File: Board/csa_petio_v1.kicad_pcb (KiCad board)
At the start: 2 copper layers, 160 x 100 mm, 99 parts, among them IC16 74LVC8T245SO24, J1 DIN-6, J11 Conn_01x09, J12 Conn_01x09, J14 Extended_PET_keyboard_connect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, J2 Conn_01x23, P1 PETUSERPORT, P2 IEEE488FLATCABLE, P4 CSABUS, P5 CBMTAPE, U1 XC6SLX9-TQG144, U10 74LS06, U11 SN74LVC245APW, U12 4051, U13 4051, U14 74LVC1G04, U15 ADM560, U16 LSF0204Q, U17 LSF0204Q, U18 LSF0204Q, U19 LSF0204Q, U2 SN74LVC245APW, U21 74LVC1G125, U22 74LVC1G125, U23 74LVC1G00, U3 SN74LVC245APW, U4 SN75160BDW, U5 SN75161BDW, U6 LSF0204Q, U7 LSF0204Q, U8 LSF0204Q, U9 LSF0204Q, X3 M09HPS

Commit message: start working on 1.0b
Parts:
- IC16: footprint Package_SO:TSSOP-24_6.1x7.8mm_P0.65mm -> Package_SO:TSSOP-24_4.4x7.8mm_P0.65mm
- R5: value 4k7 -> 10k
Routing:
- net GND: track 943.6 -> 945.3 mm
- net VCC: track 754.8 -> 755.7 mm
- net R/-W: track 54.5 -> 55.3 mm
- net Net-(IC16-B8): track 32.4 -> 33.2 mm
- net Net-(IC16-B7): track 31.6 -> 32.4 mm
- net Net-(IC16-B6): track 29.0 -> 29.9 mm
- net Net-(IC16-B5): track 27.9 -> 28.8 mm
- net Net-(IC16-B4): track 26.9 -> 27.8 mm
- net Net-(IC16-B3): track 24.9 -> 25.7 mm
- net Net-(IC16-B2): track 24.0 -> 24.9 mm
- net Net-(IC16-B1): track 25.2 -> 26.0 mm
- net D7: track 18.2 -> 19.1 mm
- net D6: track 18.0 -> 18.9 mm
- net D5: track 18.0 -> 18.8 mm
- net D4: track 18.3 -> 19.2 mm
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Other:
- board text added: "CSA-CBMIO-V1.0B"
- board text removed: "CSA-CBMIO-V1.0A"

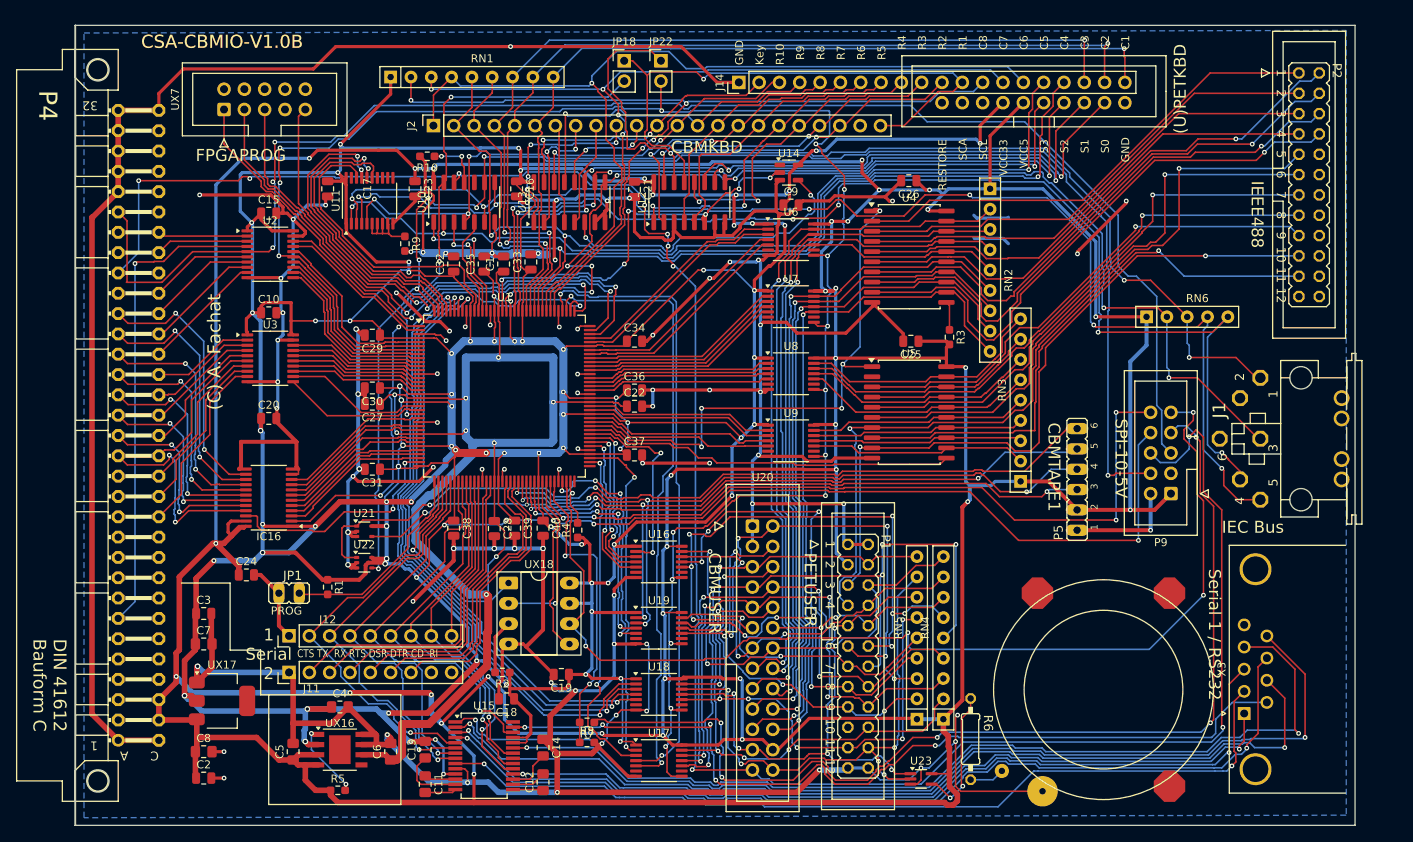
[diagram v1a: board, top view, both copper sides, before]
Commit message: schem draft done, layout work started
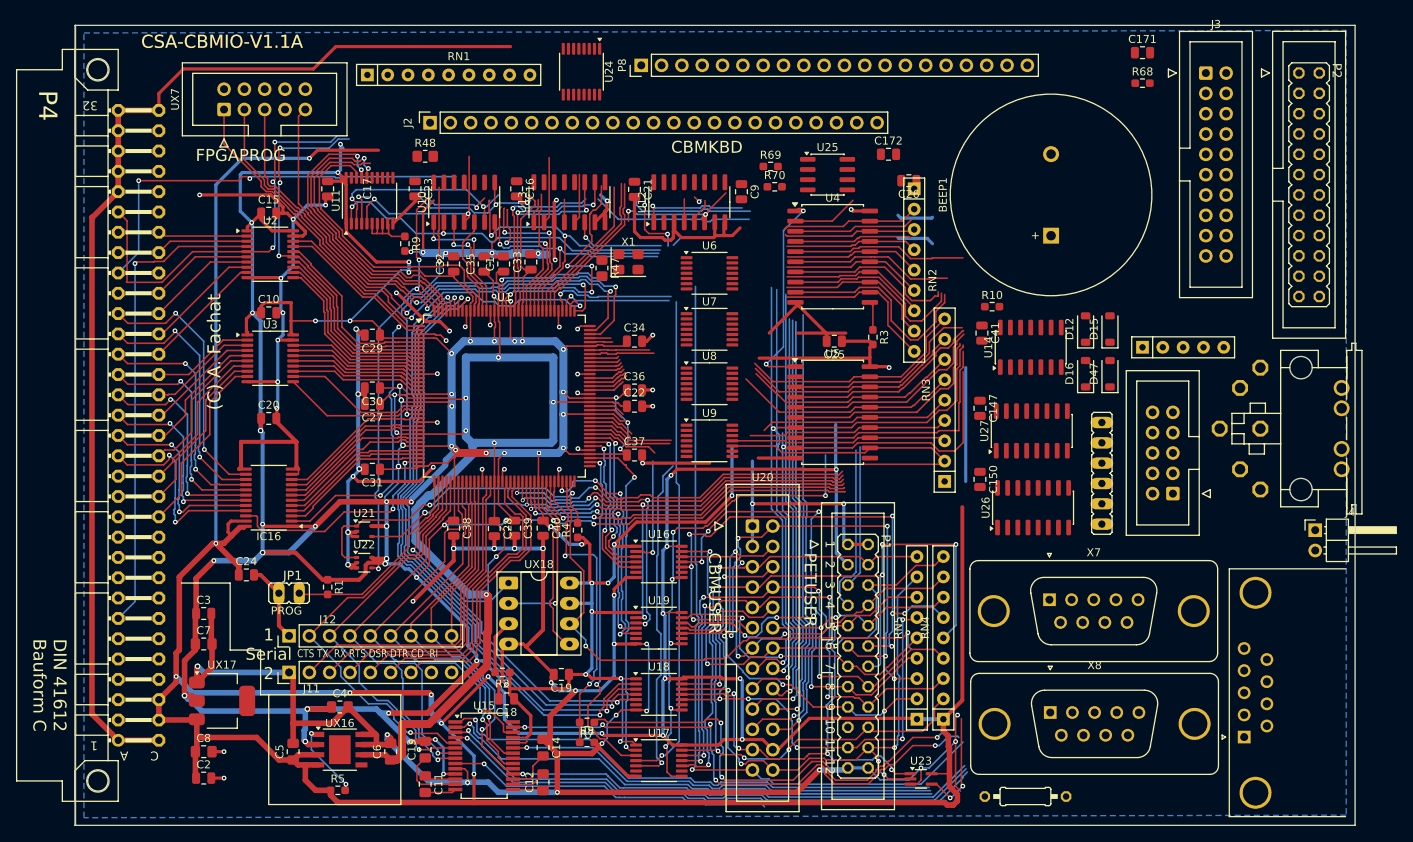
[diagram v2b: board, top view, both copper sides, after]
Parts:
- removed J14: Extended_PET_keyboard_connector, csa_petio_v1:PET_Extended_Keyboard_Connector
- removed JP18, JP22: JP1E, Connector_PinHeader_2.54mm:PinHeader_1x02_P2.54mm_Vertical
- added C147: 0.1u, Capacitor_SMD:C_0805_2012Metric, F.Cu at (181.6, 102.9)
- added C150: 0.1u, Capacitor_SMD:C_0805_2012Metric, F.Cu at (181.6, 111.8)
- added C171: 51pF, Capacitor_SMD:C_0805_2012Metric, F.Cu at (201.9, 58.4)
- added C172: 360p, Capacitor_SMD:C_0805_2012Metric, F.Cu at (170.2, 71.1)
- added C41: 100n, Capacitor_SMD:C_0805_2012Metric, F.Cu at (181.9, 93.5)
- added D12: 1N4448, Diode_SMD:D_SOD-123, F.Cu at (194.8, 93.0)
- added D15: 1N4448, Diode_SMD:D_SOD-123, F.Cu at (197.9, 93.0)
- added D16: 1N4448, Diode_SMD:D_SOD-123, F.Cu at (194.8, 98.6)
- added D47: 1N4448, Diode_SMD:D_SOD-123, F.Cu at (197.9, 98.6)
- added J3: New_PET_keyboard_connector, Connector_IDC:IDC-Header_2x10_P2.54mm_Vertical, F.Cu at (209.8, 61.0)
- added J4: Conn_01x02, Connector_PinHeader_2.54mm:PinHeader_1x02_P2.54mm_Horizontal, F.Cu at (223.5, 118.1)
- added P8: ~, Connector_PinHeader_2.54mm:PinHeader_1x20_P2.54mm_Vertical, F.Cu at (139.3, 60.0)
- added R47: 4k7, Resistor_SMD:R_0805_2012Metric_Pad1.20x1.40mm_HandSolder, F.Cu at (134.4, 85.3)
- added R48: 4k7, Resistor_SMD:R_0805_2012Metric_Pad1.20x1.40mm_HandSolder, F.Cu at (112.3, 71.4)
- added R68: 1M, Resistor_SMD:R_0603_1608Metric_Pad0.98x0.95mm_HandSolder, F.Cu at (201.9, 62.2)
- added R69: 1M, Resistor_SMD:R_0603_1608Metric_Pad0.98x0.95mm_HandSolder, F.Cu at (155.4, 72.6)
- added R70: 47k, Resistor_SMD:R_0603_1608Metric_Pad0.98x0.95mm_HandSolder, F.Cu at (156.0, 75.2)
- added U24: 74LVC165, Package_SO:TSSOP-16_4.4x5mm_P0.65mm, F.Cu at (131.8, 60.8)
- added U25: NE555D, Package_SO:SOIC-8_3.9x4.9mm_P1.27mm, F.Cu at (162.6, 73.7)
- added U26: CD4053B, Package_SO:SOIC-16_3.9x9.9mm_P1.27mm, F.Cu at (188.2, 115.3)
- added U27: CD4053B, Package_SO:SOIC-16_3.9x9.9mm_P1.27mm, F.Cu at (188.1, 105.7)
- added X1: 18.432MHz, Oscillator:Oscillator_SMD_SeikoEpson_SG8002CE-4Pin_3.2x2.5mm, F.Cu at (137.7, 84.6)
- added X7: M09-182, Connector_Dsub:DSUB-9_Pins_Vertical_P2.77x2.84mm_MountingHoles, F.Cu at (190.3, 126.8)
- added X8: M09-182, Connector_Dsub:DSUB-9_Pins_Vertical_P2.77x2.84mm_MountingHoles, F.Cu at (190.4, 140.9)
- BEEP1: footprint csa_petio_v1:PIEZOBEEPER -> Buzzer_Beeper:MagneticBuzzer_StarMicronics_TMX-H
- R10, R3, R9: value 1k -> 4k7
- U14: value 74LVC1G04 -> 74LS06; footprint Package_TO_SOT_SMD:SOT-23-5 -> Package_SO:SO-14_3.9x8.65mm_P1.27mm
- moved R10 73.1 mm to (183.1, 90.2), turned to 0 degrees
- moved BEEP1 57.1 mm to (190.5, 81.3)
- moved U14 37.3 mm to (188.0, 95.2), turned to 90 degrees
- moved U6 11.0 mm to (147.8, 86.0)
- moved U7 10.6 mm to (147.8, 93.0)
- moved U8 10.3 mm to (147.8, 99.8)
- moved U9 10.2 mm to (147.8, 106.9)
- moved R6 9.93 mm to (187.3, 151.4), turned to 0 degrees
- moved R3 9.57 mm to (168.2, 94.0)
- moved U4 9.57 mm to (163.2, 83.9)
- moved U5 9.57 mm to (163.2, 103.4)
- moved C25 9.57 mm to (163.4, 94.5)
- moved RN2 9.49 mm to (173.4, 75.4)
- moved RN3 9.49 mm to (177.2, 112.0)
- moved C9 6.41 mm to (151.8, 75.8), turned to -90 degrees
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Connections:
- net Net-(P1-PA0) renamed PUP0
- net Net-(P1-PA1) renamed PUP1
- net Net-(P1-PA2) renamed PUP2
- net Net-(P1-PA3) renamed PUP3
- net Net-(P1-PA4) renamed PUP4
- net Net-(P1-PA5) renamed PUP5
- net Net-(P1-PA6) renamed PUP6
- net Net-(P1-PA7) renamed PUP7
- P4 pad A23: unconnected-(P4-/NMI-PadA23) -> /BNMI
- R10 pad 1: Net-(R10-Pad1) -> VCC
- R10 pad 2: GND -> Net-(R10-Pad2)
- RN1 pad 2: Net-(RN1-R1) -> Net-(J3-C8)
- RN1 pad 3: Net-(RN1-R2) -> Net-(J3-C7)
- U1 pad 1: PHI2 -> /IRQ
- U1 pad 114: Net-(RN1-R1) -> unconnected-(U1A-IO_L65N_SCP2_0-Pad114)
- U1 pad 115: Net-(RN1-R2) -> unconnected-(U1A-IO_L65P_SCP3_0-Pad115)
- U1 pad 116: Net-(J2-Pin_1) -> UP14
- U1 pad 117: Net-(J2-Pin_2) -> Net-(U1A-IO_L64P_SCP5_0)
- U1 pad 118: Net-(J2-Pin_3) -> Net-(U1A-IO_L63N_SCP6_0)
- U1 pad 119: Net-(J2-Pin_4) -> Net-(U1A-IO_L63P_SCP7_0)
- U1 pad 120: Net-(J2-Pin_5) -> Net-(U1A-IO_L62N_VREF_0)
- U1 pad 121: Net-(J2-Pin_6) -> Net-(U1A-IO_L62P_0)
- U1 pad 23: /IRQ -> PHI2
- U10 pad 10: unconnected-(U10-Pad10) -> Net-(U13-Inh)
- U10 pad 11: Net-(R10-Pad1) -> KSEL3
- U14 pad 1: (no net) -> Net-(U1A-IO_L64P_SCP5_0)
- U14 pad 2: KSEL3 -> NDAC
- U14 pad 3: GND -> Net-(U1A-IO_L64P_SCP5_0)
- U14 pad 4: Net-(U13-Inh) -> NRFD
- U14 pad 5: V33 -> Net-(U25-Q)
- UX7 pad 10: (no net) -> GND
- UX7 pad 2: (no net) -> GND
- UX7 pad 4: (no net) -> V33
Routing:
- net VCC: track 755.7 -> 519.0 mm, vias 33 -> 19
- net V33: track 885.9 -> 685.4 mm, vias 81 -> 65
- net GND: track 945.3 -> 749.8 mm, vias 82 -> 68
- net /BRES: track 189.5 -> 51.9 mm
- net CLKOUT: track 188.1 -> 62.5 mm, vias 7 -> 4
- net Net-(J2-Pin_2): track 122.1 -> 0.00 mm, vias 3 -> 0
- net Net-(J2-Pin_3): track 121.2 -> 0.00 mm, vias 3 -> 0
- net /RES: track 230.2 -> 110.6 mm, vias 16 -> 9
- net /IO2/FASTCLK: track 143.4 -> 24.4 mm, vias 5 -> 2
- net /IO2/DATA: track 160.4 -> 41.8 mm, vias 6 -> 2
- net Net-(J2-Pin_1): track 117.1 -> 0.00 mm, vias 1 -> 0
- net Net-(J2-Pin_4): track 116.1 -> 0.00 mm, vias 3 -> 0
- net Net-(J2-Pin_5): track 115.5 -> 0.00 mm, vias 3 -> 0
- net /BIRQ: track 273.2 -> 158.8 mm, vias 10 -> 5
- net /IO2/SLOWCLK: track 161.6 -> 50.6 mm, vias 6 -> 2
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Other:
- board text added: "CSA-CBMIO-V1.1A"
- board text removed: "(U)PETKBD"
- board text removed: "CBMTAPE1"
- board text removed: "CSA-CBMIO-V1.0B"
- board text removed: "IEC Bus"
- board text removed: "IEEE488"
- board text removed: "SPI-10-5V"
- board text removed: "Serial 1 / RS232"

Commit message: more layout work
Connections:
- X8 pad 1: UP4 -> PUP4
- X8 pad 2: UP5 -> PUP5
- X8 pad 3: UP6 -> PUP6
- X8 pad 4: UP7 -> PUP7
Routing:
- net GND: track 749.8 -> 933.3 mm, vias 68 -> 89
- net /BNMI: track 0.00 -> 132.2 mm, vias 0 -> 1
- net V33: track 685.4 -> 812.5 mm, vias 65 -> 76
- net VCC: track 519.0 -> 626.0 mm, vias 19 -> 23
- net /BIRQ: track 158.8 -> 259.2 mm, vias 5 -> 11
- net /IRQ: track 0.00 -> 96.2 mm, vias 0 -> 3
- net /RES: track 110.6 -> 205.0 mm, vias 9 -> 19
- net PUP5: track 68.6 -> 146.0 mm, vias 4 -> 8
- net Net-(BEEP1-+): track 0.00 -> 76.9 mm
- net Net-(J2-Pin_2): track 0.00 -> 76.0 mm, vias 0 -> 2
- net /BRES: track 51.9 -> 127.8 mm
- net Net-(J2-Pin_1): track 0.00 -> 74.7 mm, vias 0 -> 2
- net Net-(J2-Pin_6): track 0.00 -> 72.5 mm, vias 0 -> 2
- net Net-(J2-Pin_5): track 0.00 -> 71.9 mm, vias 0 -> 2
- net Net-(J2-Pin_3): track 0.00 -> 71.8 mm, vias 0 -> 2
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
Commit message: cbmio 1.1a draft
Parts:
- C147, C150: value 0.1u -> 100n
- R47, R48: footprint Resistor_SMD:R_0805_2012Metric_Pad1.20x1.40mm_HandSolder -> Resistor_SMD:R_0603_1608Metric_Pad0.98x0.95mm_HandSolder
- moved C171 37.0 mm to (168.7, 74.7), turned to 180 degrees
- moved R68 29.1 mm to (173.4, 67.8)
- moved C26 2.45 mm to (173.6, 72.1)
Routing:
- net VCC: track 626.0 -> 948.0 mm, vias 23 -> 40
- net GND: track 933.3 -> 1162.0 mm, vias 89 -> 102
- net /RES: track 205.0 -> 329.9 mm, vias 19 -> 22
- net V33: track 812.5 -> 917.5 mm, vias 76 -> 83
- net /IO2/SATN: track 56.6 -> 151.2 mm, vias 2 -> 5
- net /IO2/SLOWCLK: track 58.2 -> 147.0 mm, vias 2 -> 4
- net NDAC: track 24.8 -> 105.8 mm, vias 0 -> 3
- net DIO1: track 8.27 -> 81.1 mm, vias 0 -> 2
- net NRFD: track 26.1 -> 98.2 mm, vias 0 -> 3
- net DIO5: track 20.3 -> 92.3 mm, vias 0 -> 2
- net DIO7: track 23.6 -> 95.2 mm, vias 0 -> 1
- net DIO8: track 26.8 -> 98.1 mm, vias 0 -> 1
- net DIO6: track 21.0 -> 92.1 mm, vias 0 -> 1
- net /BRES: track 127.8 -> 195.4 mm, vias 3 -> 6
- net /IO2/DATA: track 86.9 -> 154.4 mm, vias 2 -> 4
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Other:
- board text added: "G UCPU VS"
- board text added: "IEEE488"
- board text added: "Joy 1"
- board text added: "Joy 2"
- board text added: "PET KBD"
- board text added: "RS232"
- board text added: "SIEC"
- board text added: "UEXT"
- board text added: "UPET KBD"

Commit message: as submitted
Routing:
- net V33: track 917.5 -> 918.3 mm
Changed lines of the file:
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@@
 				(font
 					(size 1.27 1.27)
+					(thickness 0.15)
 				)
 			)
@@
 				(font
 					(size 1.27 1.27)
+					(thickness 0.15)
 				)
 			)
@@
 				(font
 					(size 1.27 1.27)
+					(thickness 0.15)
 				)
 			)
@@
 				(font
 					(size 1.27 1.27)
+					(thickness 0.15)
 				)
 			)
@@
 				(font
 					(size 1.27 1.27)
+					(thickness 0.15)
 				)
 			)
@@
 				(font
 					(size 1.27 1.27)
+					(thickness 0.15)
 				)
 			)
@@
 				(font
 					(size 1.27 1.27)
+					(thickness 0.15)
 				)
 			)
@@
 				(font
 					(size 1.27 1.27)
+					(thickness 0.15)
 				)
 			)
@@
 				(font
 					(size 1.27 1.27)
+					(thickness 0.15)
 				)
 			)
@@
 				(font
 					(size 1.27 1.27)
+					(thickness 0.15)
 				)
 			)
@@
 				(font
 					(size 1.27 1.27)
+					(thickness 0.15)
 				)
 			)
@@
 				(font
 					(size 1.27 1.27)
+					(thickness 0.15)
 				)
 			)
@@
 				(font
 					(size 1.27 1.27)
+					(thickness 0.15)
 				)
 			)
@@
 				(font
 					(size 1.27 1.27)
+					(thickness 0.15)
 				)
 			)
@@
 				(font
 					(size 1.27 1.27)
+					(thickness 0.15)
 				)
 			)
@@
 				(font
 					(size 1.27 1.27)
+					(thickness 0.15)
 				)
 			)
@@
 				(font
 					(size 1.27 1.27)
+					(thickness 0.15)
 				)
 			)
@@
 			)
 		)
-		(property "LCSC" "C25687202"
+		(property "LCSC" "C50981"
 			(at 0 0 0)
 			(layer "F.SilkS")
@@
 				(font
 					(size 1.27 1.27)
+					(thickness 0.15)
 				)
 			)
@@
 				(font
 					(size 1.27 1.27)
+					(thickness 0.15)
 				)
 			)
@@
 				(font
 					(size 1.27 1.27)
+					(thickness 0.15)
 				)
 			)
@@
 	)
 	(via
+		(at 110.744 70.612)
+		(size 0.6)
+		(drill 0.3)
+		(layers "F.Cu" "B.Cu")
+		(net "V33")
+	)
+	(via
 		(at 122.174 108.458)
 		(size 0.6)
@@
 	)
 	(via
-		(at 110.3376 70.2056)
-		(size 0.6)
-		(drill 0.3)
-		(layers "F.Cu" "B.Cu")
-		(net "V33")
-	)
-	(via
 		(at 82.188648 138.791352)
 		(size 0.7)
@@
 	)
 	(segment
+		(start 123.698 72.644)
+		(end 112.776 72.644)
+		(width 0.4)
+		(layer "B.Cu")
+		(net "V33")
+	)
+	(segment
 		(start 147.574 90.932)
 		(end 147.574 84.566934)
@@
 	)
 	(segment
-		(start 112.776 72.644)
-		(end 111.268 71.136)
-		(width 0.4)
-		(layer "B.Cu")
-		(net "V33")
-	)
-	(segment
 		(start 129.056 72.006)
 		(end 129.8684 72.8184)
@@
 	)
 	(segment
+		(start 112.776 72.644)
+		(end 110.744 70.612)
+		(width 0.4)
+		(layer "B.Cu")
+		(net "V33")
+	)
+	(segment
 		(start 122.428 137.414)
 		(end 119.454655 134.440655)
@@
 		(layer "B.Cu")
 		(net "V33")
-	)
-	(segment
-		(start 123.698 72.644)
-		(end 112.776 72.644)
-		(width 0.4)
-		(layer "B.Cu")
-		(net "V33")
